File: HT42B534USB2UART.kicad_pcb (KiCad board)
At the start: 2 copper layers, 27.9 x 21.6 mm, 14 parts, among them J1 USB_A, J2 Conn_01x06, U1 HT42B534_8SOP

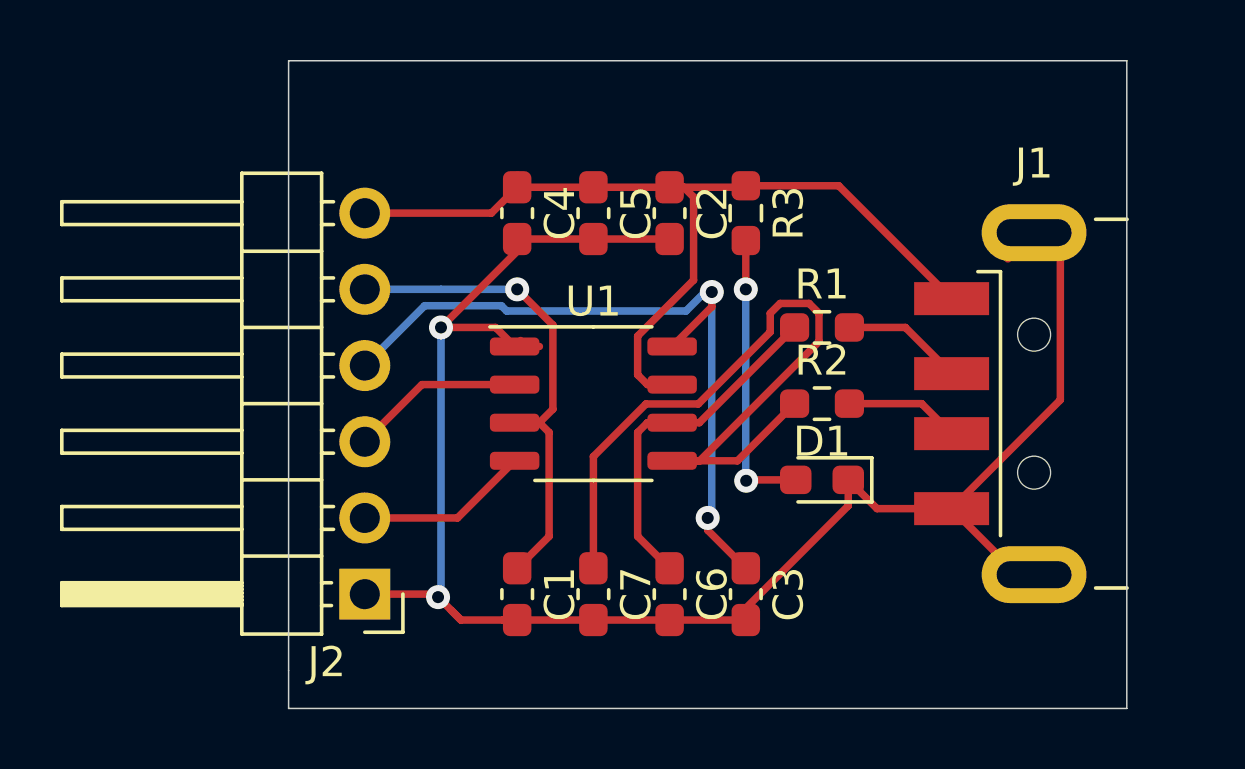
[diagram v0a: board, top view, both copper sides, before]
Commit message: Setup board parameters(track width, via size etc) and use filled Cu layers
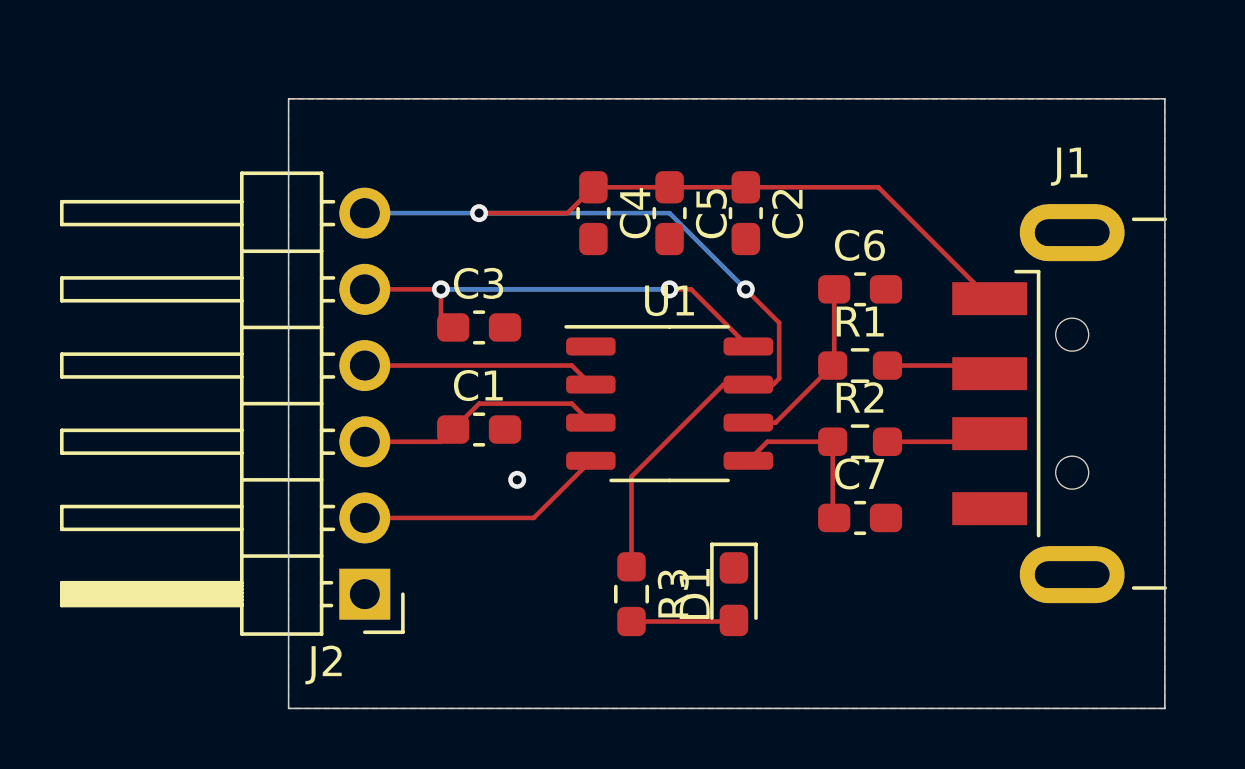
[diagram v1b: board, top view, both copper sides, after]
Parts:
- moved R3 13.3 mm to (80.0, 96.5)
- moved C3 12.6 mm to (74.9, 87.6), turned to 0 degrees
- moved C6 12.0 mm to (87.6, 86.4), turned to 0 degrees
- moved C7 9.25 mm to (87.6, 94.0), turned to 0 degrees
- moved C1 5.63 mm to (74.9, 91.0), turned to 0 degrees
- moved D1 4.81 mm to (83.4, 96.5), turned to 270 degrees
- moved C5 2.54 mm to (81.3, 83.8)
- moved U1 2.54 mm to (81.3, 90.2)
- moved C2 2.54 mm to (83.8, 83.8)
- moved C4 2.54 mm to (78.7, 83.8)
- moved R1 1.80 mm to (87.6, 88.9)
- moved R2 1.80 mm to (87.6, 91.4)
- moved J1 1.27 mm to (101.6, 90.2)
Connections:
- J2 pad 3: /TX -> VDDA
- J2 pad 4: /V33O -> /TX
- J2 pad 5: VDDA -> /V33O
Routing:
- net GND: track 62.9 -> 0.00 mm, vias 2 -> 1
- net /D+: track 26.2 -> 5.64 mm
- net VDD: track 30.8 -> 45.4 mm, vias 0 -> 3
- net /V33O: track 25.0 -> 15.0 mm
- net VDDA: track 16.5 -> 8.32 mm, vias 1 -> 0
- net Net-(D1-Pad2): track 9.68 -> 3.43 mm, vias 2 -> 0
- net /D-: track 11.7 -> 6.16 mm
- net /RX: track 5.78 -> 8.32 mm
- net /TX: track 5.78 -> 7.80 mm
- net Net-(J1-Pad2): track 4.05 -> 3.52 mm
- added copper zone on B.Cu, net GND
- added copper zone on F.Cu, net GND
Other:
- board size 27.9 x 21.6 mm -> 29.2 x 20.3 mm
- net class Default: clearance 0.2 -> 0.127; trace_width 0.25 -> 0.1524; via_dia 0.8 -> 0.6; via_drill 0.4 -> 0.3
- rule trace_clearance: 0.2 -> 0.127
- rule trace_min: 0.2 -> 0.1524
- rule via_min_size: 0.4 -> 0.6

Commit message: Add slik text
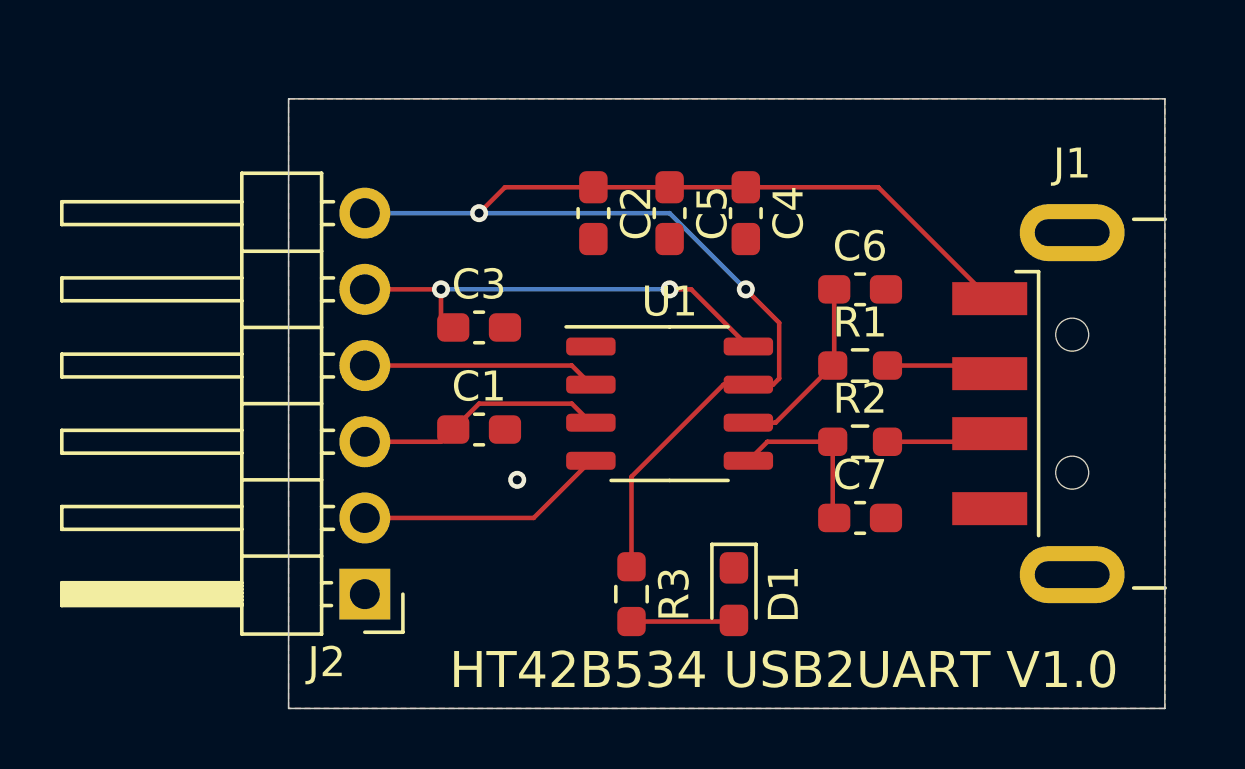
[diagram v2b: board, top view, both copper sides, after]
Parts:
- moved C2 5.08 mm to (78.7, 83.8)
- moved C4 5.08 mm to (83.8, 83.8)
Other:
- board text added: "GND"
- board text added: "HT42B534 USB2UART V1.0"
- board text added: "RX"
- board text added: "TX"
- board text added: "V33O"
- board text added: "VDD"
- board text added: "VDDIO"

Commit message: Add a conn01x03 for voltage selection
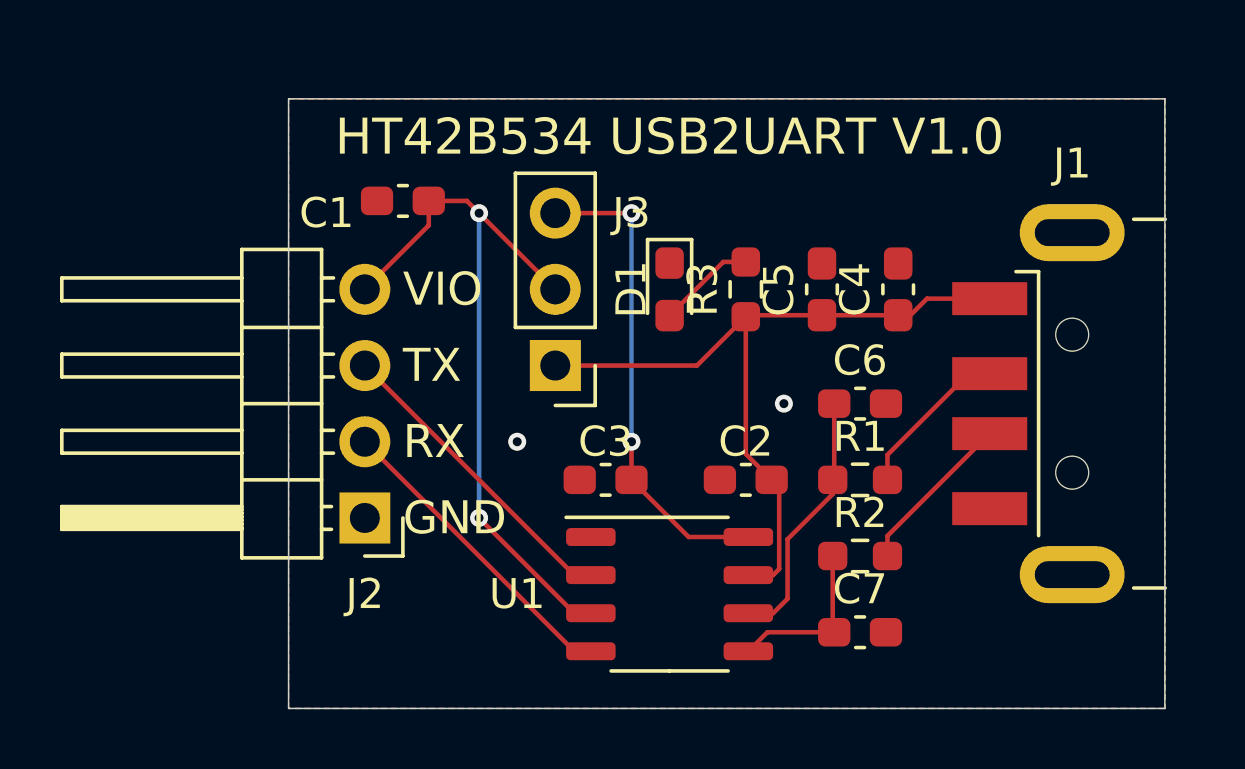
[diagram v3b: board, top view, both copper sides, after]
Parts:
- added J3: Conn_01x03, Connector_PinHeader_2.54mm:PinHeader_1x03_P2.54mm_Vertical, F.Cu at (77.5, 88.9)
- J2: value Conn_01x06 -> Conn_01x04; footprint Connector_PinHeader_2.54mm:PinHeader_1x06_P2.54mm_Horizontal -> Connector_PinHeader_2.54mm:PinHeader_1x04_P2.54mm_Horizontal
- moved R3 10.9 mm to (83.8, 86.4), turned to 90 degrees
- moved D1 10.4 mm to (81.3, 86.4)
- moved C2 10.2 mm to (83.8, 92.7), turned to 180 degrees
- moved C1 8.03 mm to (72.4, 83.4), turned to 180 degrees
- moved C3 6.60 mm to (79.1, 92.7), turned to 180 degrees
- moved U1 6.35 mm to (81.3, 96.5)
- moved C4 5.68 mm to (88.9, 86.4), turned to 90 degrees
- moved C5 5.68 mm to (86.4, 86.4), turned to 90 degrees
- moved C6 3.81 mm to (87.6, 90.2)
- moved C7 3.81 mm to (87.6, 97.8)
- moved R2 3.81 mm to (87.6, 95.2)
- moved R1 3.81 mm to (87.6, 92.7)
- moved J2 2.54 mm to (71.1, 94.0)
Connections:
- J2 pad 3: VDDA -> /TX
- J2 pad 4: /TX -> VDDA
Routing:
- net VDD: track 45.4 -> 25.4 mm, vias 3 -> 0
- net VDDA: track 8.32 -> 24.5 mm, vias 0 -> 2
- net /TX: track 7.80 -> 10.4 mm
- net /D-: track 6.16 -> 8.71 mm
- net /RX: track 8.32 -> 10.4 mm
- net Net-(J1-Pad3): track 3.52 -> 5.49 mm
- net Net-(J1-Pad2): track 3.52 -> 5.36 mm
- net /V33O: track 15.0 -> 16.1 mm
- net GND: vias 1 -> 2
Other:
- board text added: "VIO"
- board text removed: "VDDIO"

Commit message: Kicad 6.0
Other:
- net class Default removed
